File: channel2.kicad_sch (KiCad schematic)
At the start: 58 parts, among them IC3 TLV73325PDBVT, IC4 TLV73312PDBVT, J4 47151-1001, J5 5051101992, U4 TC358742XBG, U5 TPD8S009DSMR, U6 PCA9517ATP, Y2 7C-27.000MBB-T

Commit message: [#58304] Perform globlib
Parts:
- C24, C25, C26, C31, C32, C33, C34, C35, C37, C38, C45: footprint antmicro-hdmi-mipi-bridge-hw-footprints:C_0402_1005Metric -> antmicro-footprints:C_0402_1005Metric; symbol antmicro-hdmi-mipi-bridge-hw:C_100n_0402 -> antmicroCapacitors0402:C_100n_0402
- C36, C39, C44, C46: footprint antmicro-hdmi-mipi-bridge-hw-footprints:C_0402_1005Metric -> antmicro-footprints:C_0402_1005Metric; symbol antmicro-hdmi-mipi-bridge-hw:C_47p_0402 -> antmicroCapacitors0402:C_47p_0402
- C40, C41, C42, C43: footprint antmicro-hdmi-mipi-bridge-hw-footprints:C_0603_1608Metric -> antmicro-footprints:C_0603_1608Metric; symbol antmicro-hdmi-mipi-bridge-hw:C_10u_0603 -> antmicroCapacitors0603:C_10u_0603
- C47, C48, C49, C50: footprint antmicro-hdmi-mipi-bridge-hw-footprints:C_0402_1005Metric -> antmicro-footprints:C_0402_1005Metric; symbol antmicro-hdmi-mipi-bridge-hw:C_470p_0402 -> antmicroCapacitors0402:C_470p_0402
- C51, C52, C53, C54: footprint antmicro-hdmi-mipi-bridge-hw-footprints:C_0603_1608Metric -> antmicro-footprints:C_0603_1608Metric; symbol antmicro-hdmi-mipi-bridge-hw:C_4u7_0603 -> antmicroCapacitors0603:C_4u7_0603
- FB10, FB11, FB8, FB9: footprint antmicro-hdmi-mipi-bridge-hw-footprints:FB_0805_2012Metric -> antmicro-footprints:FB_0805_2012Metric; symbol antmicro-hdmi-mipi-bridge-hw:FB_1000Z_0.8A_0805 -> antmicroFerriteBeadsandChips:FB_1kZ_0.8A_WE-CBF_0805
- FB12: footprint antmicro-hdmi-mipi-bridge-hw-footprints:FB_0603_1608Metric -> antmicro-footprints:FB_0603_1608Metric; symbol antmicro-hdmi-mipi-bridge-hw:FB_600Z_0.5A_0603 -> antmicroFerriteBeadsandChips:FB_600Z_0.5A_Murata-BLM18AG_0603
- FB7: footprint antmicro-hdmi-mipi-bridge-hw-footprints:FB_0603_1608Metric -> antmicro-footprints:FB_0603_1608Metric; symbol antmicro-hdmi-mipi-bridge-hw:FB_120Z_3A_0603 -> antmicroFerriteBeadsandChips:FB_120Z_3A_Murata-BLM18SG_0603
- IC3: footprint antmicro-hdmi-mipi-bridge-hw-footprints:SOT-23-5 -> antmicro-footprints:SOT-23-5; symbol antmicro-hdmi-mipi-bridge-hw:TLV73325PDBVT -> antmicroPMICVoltageRegulatorsLinear:TLV73325PDBVT
- IC4: footprint antmicro-hdmi-mipi-bridge-hw-footprints:SOT-23-5 -> antmicro-footprints:SOT-23-5; symbol antmicro-hdmi-mipi-bridge-hw:TLV73312PDBVT -> antmicroPMICVoltageRegulatorsLinear:TLV73312PDBVT
- J5: footprint antmicro-hdmi-mipi-bridge-hw-footprints:5051101992 -> antmicro-footprints:5051101992; symbol antmicro-hdmi-mipi-bridge-hw:5051101992 -> antmicroFCCConnectors:5051101992
- R14, R15, R18, R19, R20, R21: footprint antmicro-hdmi-mipi-bridge-hw-footprints:R_0603_1608Metric -> antmicro-footprints:R_0603_1608Metric; symbol antmicro-hdmi-mipi-bridge-hw:R_0R_0603 -> antmicroResistors0603:R_0R_0603
- R16, R22, R23, R24, R25: footprint antmicro-hdmi-mipi-bridge-hw-footprints:R_0402_1005Metric -> antmicro-footprints:R_0402_1005Metric; symbol antmicro-hdmi-mipi-bridge-hw:R_10k_0402 -> antmicroResistors0402:R_10k_0402
- R17: footprint antmicro-hdmi-mipi-bridge-hw-footprints:R_0402_1005Metric -> antmicro-footprints:R_0402_1005Metric; symbol antmicro-hdmi-mipi-bridge-hw:R_2k_0402 -> antmicroResistors0402:R_2k_0402
- R26: footprint antmicro-hdmi-mipi-bridge-hw-footprints:R_0402_1005Metric -> antmicro-footprints:R_0402_1005Metric; symbol antmicro-hdmi-mipi-bridge-hw:R_22R_0402 -> antmicroResistors0402:R_22R_0402
- TP5, TP6, TP7, TP8: footprint antmicro-hdmi-mipi-bridge-hw-footprints:TP_SMD_0.75mm -> antmicro-footprints:TP_SMD_0.75mm; symbol antmicro-hdmi-mipi-bridge-hw:TP_0.75mm_SMD -> antmicroTestPoints:TP_0.75mm_SMD
- U4: footprint antmicro-hdmi-mipi-bridge-hw-footprints:BGA-64_8x8_6.0x6.0mm -> antmicro-footprints:BGA-64_8x8_6.0x6.0mm; symbol antmicro-hdmi-mipi-bridge-hw:TC358742XBG -> antmicroInterfaceControllers:TC358742XBG
- U5: footprint antmicro-hdmi-mipi-bridge-hw-footprints:R-PDSO-N15 -> antmicro-footprints:R-PDSO-N15; symbol antmicro-hdmi-mipi-bridge-hw:TPD8S009DSMR -> antmicroTVSDiodes:TPD8S009DSMR
- U6: footprint antmicro-hdmi-mipi-bridge-hw-footprints:SOT1069-2 -> antmicro-footprints:SOT1069-2; symbol antmicro-hdmi-mipi-bridge-hw:PCA9517ATP -> antmicroLogicTranslatorsLevelShifters:PCA9517ATP
- Y2: footprint antmicro-hdmi-mipi-bridge-hw-footprints:7C-24.000MBB-T -> antmicro-footprints:Oscillator_SMD_TXC_7C_5x3.2x1.2mm; symbol antmicro-hdmi-mipi-bridge-hw:7C-27.000MBB-T -> antmicroOscillators:Oscillator_27MHz_TXC_7C

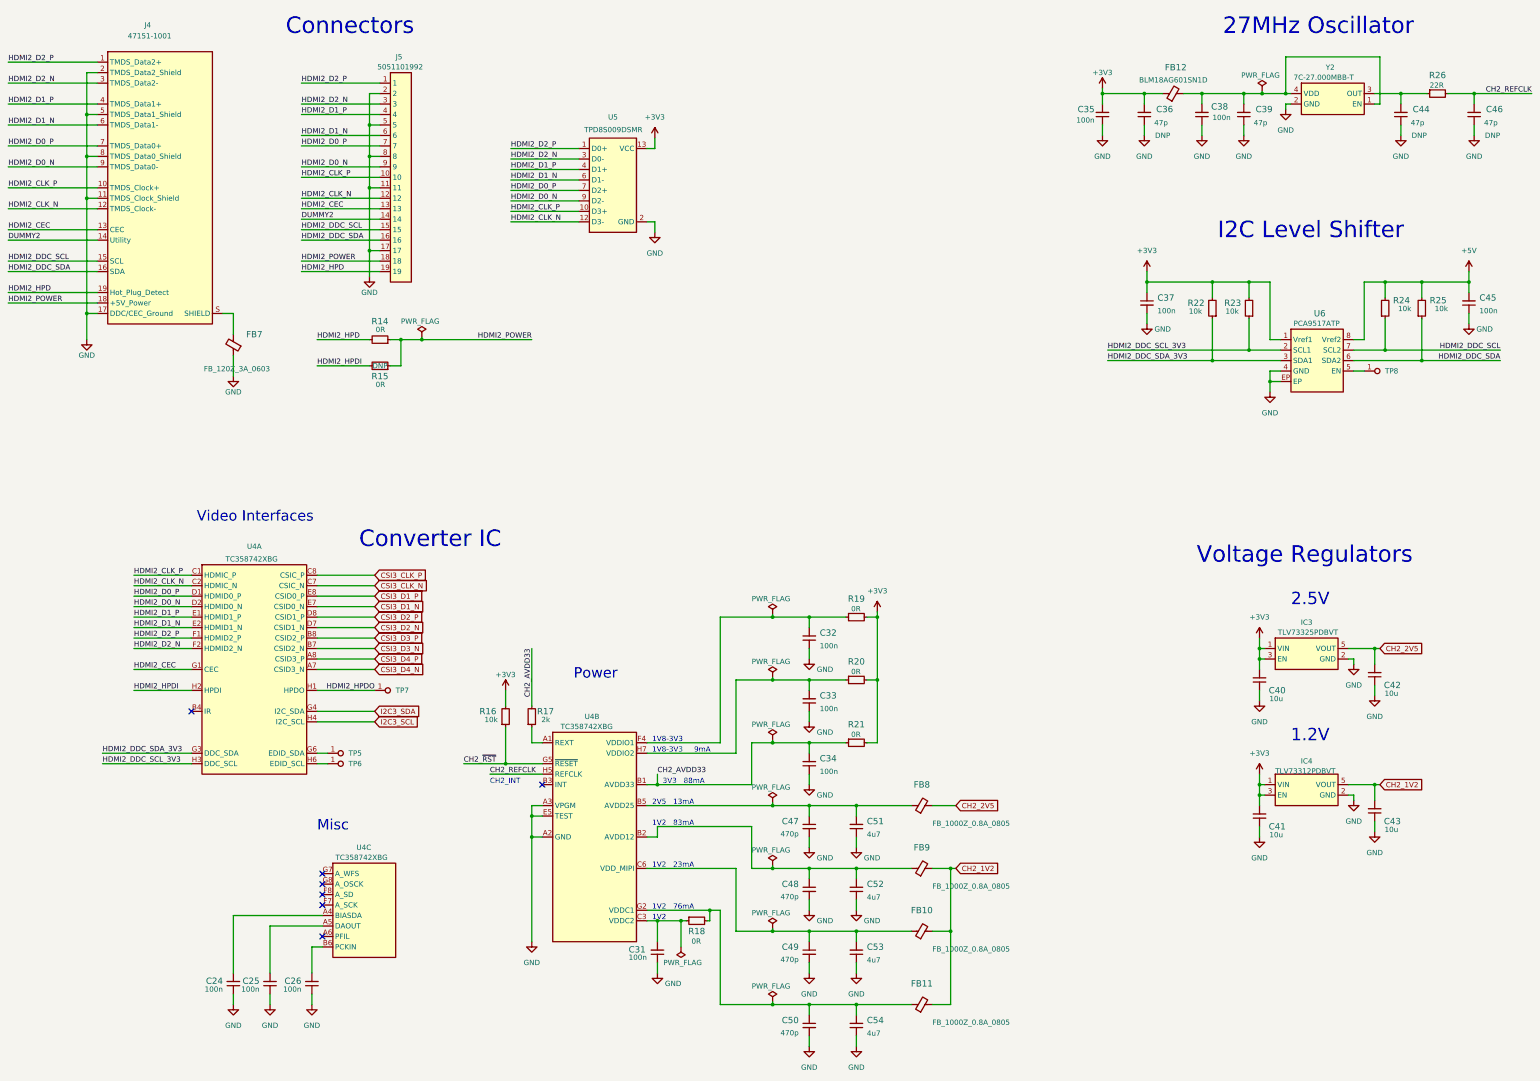
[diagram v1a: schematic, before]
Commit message: [#58304] Update symbols to global libs
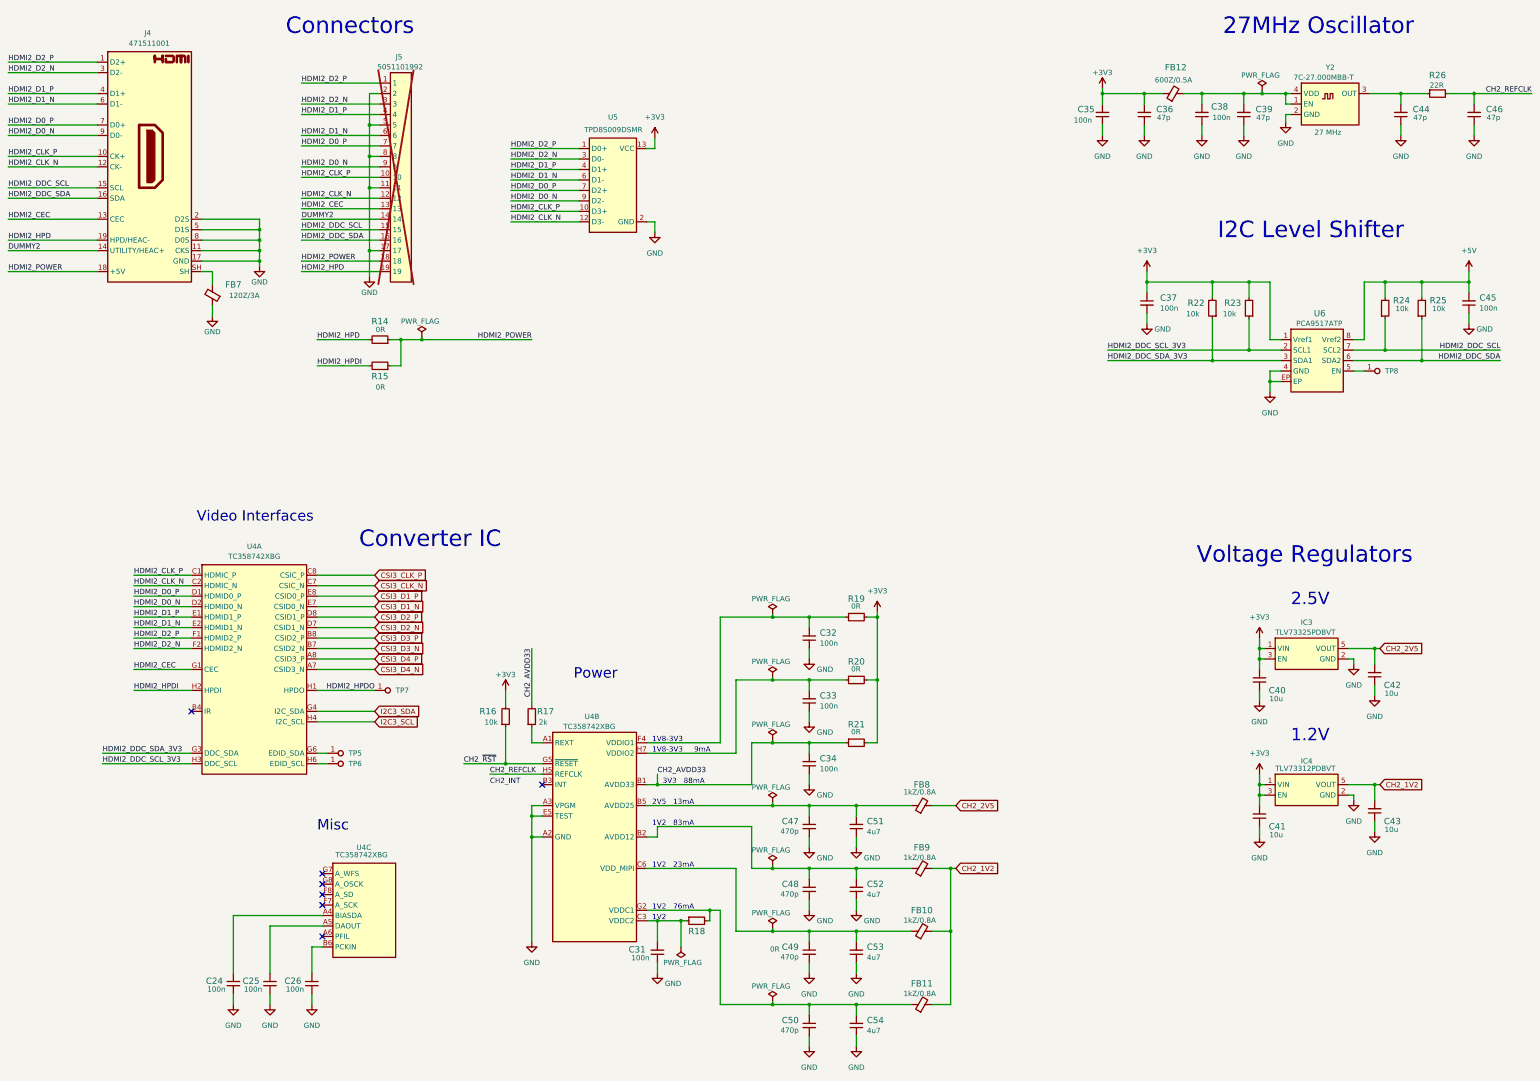
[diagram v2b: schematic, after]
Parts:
- C36, C44, C46: DNP DNP -> (none); MPN GRM1555C1E470JA01D -> C0402C470J5GACTU; Manufacturer Murata -> KEMET
- C39: MPN GRM1555C1E470JA01D -> C0402C470J5GACTU; Manufacturer Murata -> KEMET
- C40, C41, C42, C43: Dielectric (none) -> template_dielectric
- FB10, FB11, FB8, FB9: value FB_1000Z_0.8A_0805 -> FB_1kZ_0.8A_WE-CBF_0805; Val (none) -> 1kZ/0.8A
- FB12: value FB_600Z_0.5A_0603 -> FB_600Z_0.5A_Murata-BLM18AG_0603; Val (none) -> 600Z/0.5A
- FB7: value FB_120Z_3A_0603 -> FB_120Z_3A_Murata-BLM18SG_0603; Val (none) -> 120Z/3A
- J4: value 47151-1001 -> HDMI-A_Molex_471511001; footprint antmicro-hdmi-mipi-bridge-hw-footprints:47151-1001 -> antmicro-footprints:HDMI-A_Receptacle_Molex_471511001; symbol antmicro-hdmi-mipi-bridge-hw:47151-1001 -> antmicroVideoConnectors:HDMI-A_Molex_471511001; MPN 47151-1001 -> 471511001
- J5: now not fitted
- R15: DNP DNP -> (none)
- Y2: value 7C-27.000MBB-T -> Oscillator_27MHz_TXC_7C; Val (none) -> 27 MHz
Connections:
- net at FB7.2: now also J4.SH; no longer J4.S (SHIELD)
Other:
- moved on the sheet: FB7
